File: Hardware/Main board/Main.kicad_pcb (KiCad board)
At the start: 2 copper layers, 65 x 56 mm, 24 parts, among them J1 RJ12, J10 Conn_01x03, J11 Conn_01x03, J13 Conn_01x04_Male, J14 Conn_01x04_Male, J2 AudioJack3, J3 AudioJack3, J4 AudioJack3, J5 AudioJack3, J6 RJ12, J7 RJ12, J8 Conn_01x03, J9 Conn_01x03, P1 Conn_02x20_Odd_Even, U1 ADS1115IDGS, U2 PCF8574

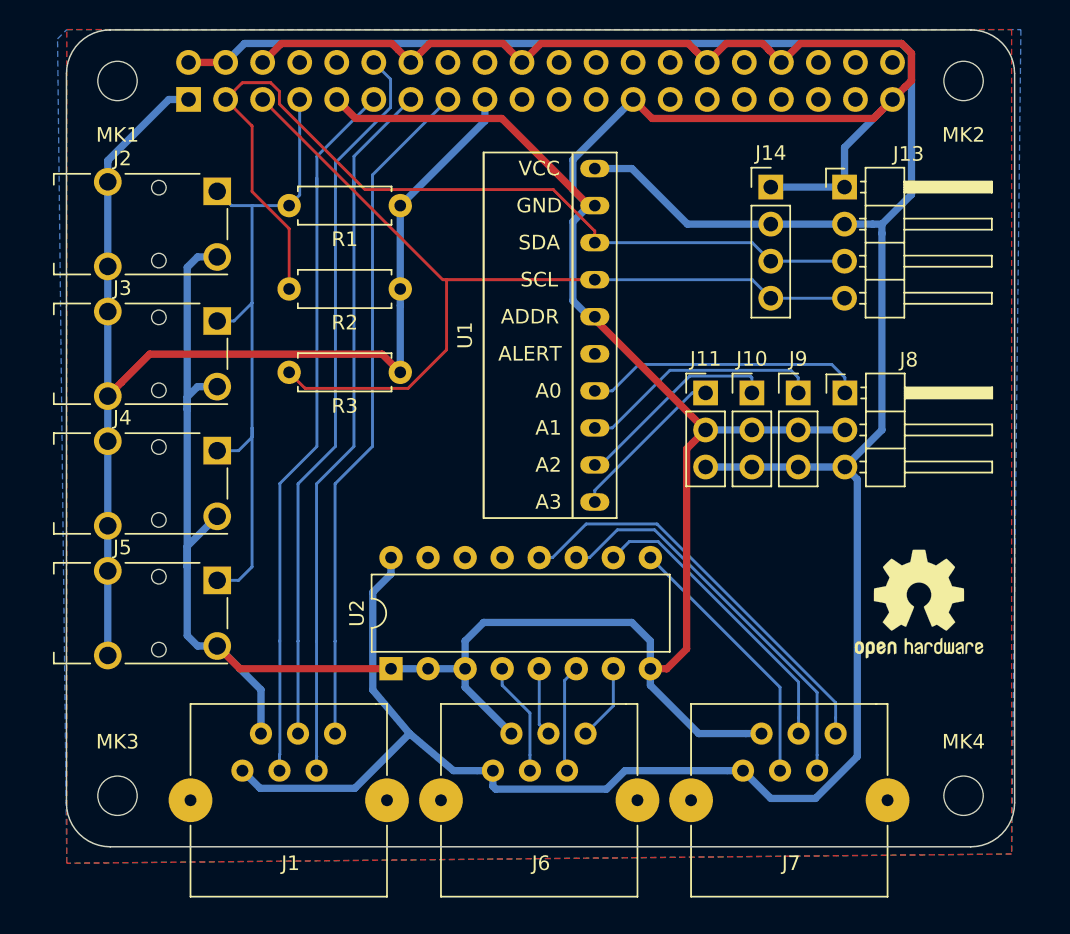
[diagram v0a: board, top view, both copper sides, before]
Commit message: Poprawki w płycie głównej
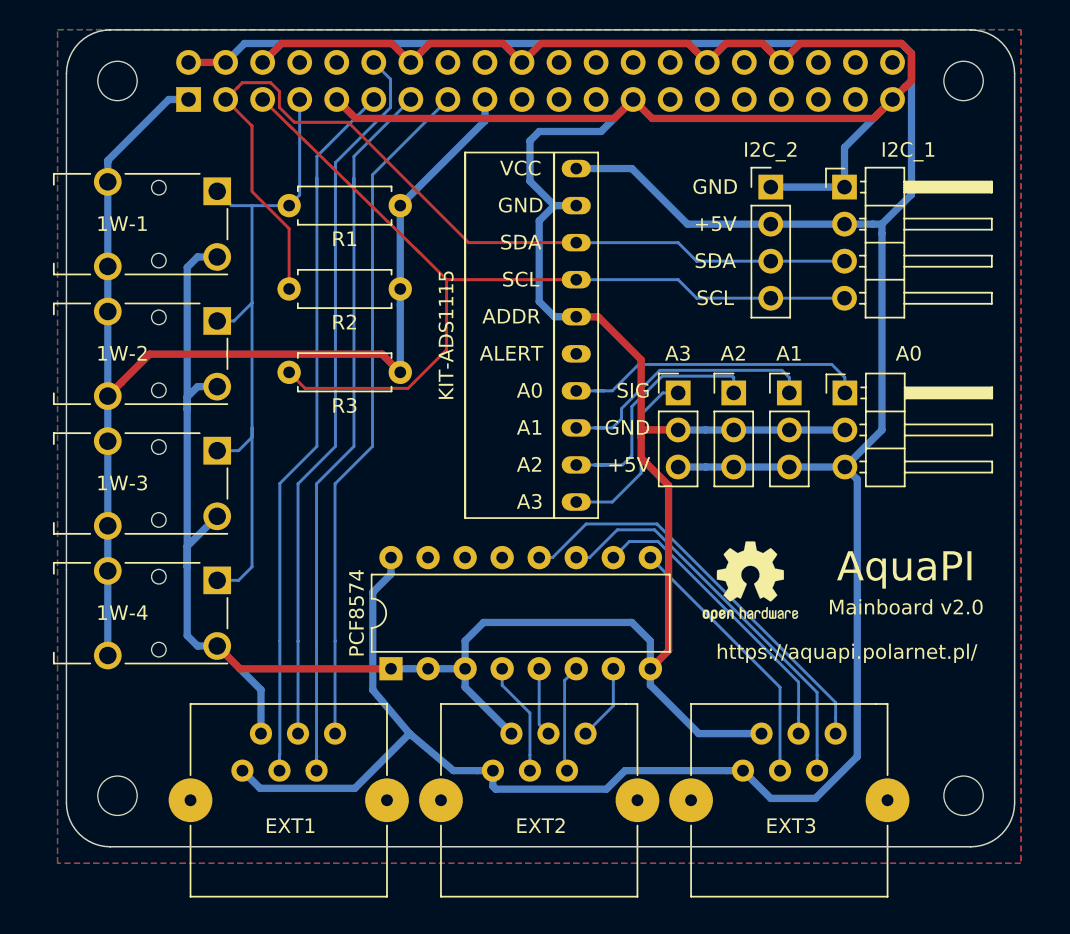
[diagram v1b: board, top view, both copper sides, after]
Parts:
- removed J6: RJ12, Connectors:RJ12_E
- removed the REF*** at (258.4, 133.3)
- added EXT2: RJ12, Connectors:RJ12_E, F.Cu at (229.2, 144.8)
- added REF***: OSHW-Logo2_7.3x6mm_SilkScreen, Symbols:OSHW-Logo2_7.3x6mm_SilkScreen, F.Cu at (246.9, 131.8)
- A0: renamed from J8; value Conn_01x03 -> ADC_A
- A1: renamed from J9; value Conn_01x03 -> ADC_B
- A2: renamed from J10; value Conn_01x03 -> ADC_C
- A3: renamed from J11; value Conn_01x03 -> ADC_D
- moved A3 1.88 mm to (241.9, 118.9)
- moved KIT-ADS1115 1.27 mm to (234.9, 114.9)
- moved A2 1.25 mm to (245.7, 118.9)
- moved A1 0.61 mm to (249.6, 118.9)
- renumbered J2 to 1W-1, J3 to 1W-2, J4 to 1W-3, J5 to 1W-4, J1 to EXT1, J7 to EXT3, J13 to I2C_1, J14 to I2C_2, U1 to KIT-ADS1115, U2 to PCF8574
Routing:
- net GND: track 258.9 -> 269.5 mm
- net Net-(A2-Pad1): track 14.4 -> 18.1 mm
- net +5V: track 193.9 -> 197.1 mm
- net Net-(A0-Pad1): track 19.3 -> 21.2 mm
- net Net-(A1-Pad1): track 16.8 -> 18.5 mm
- net Net-(A3-Pad1): track 11.2 -> 12.4 mm
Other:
- board text added: "+5V"
- board text added: "AquaPI"
- board text added: "GND"
- board text added: "Mainboard v2.0"
- board text added: "SCL"
- board text added: "SDA"
- board text added: "SIG"
- board text added: "https://aquapi.polarnet.pl/"

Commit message: nowy projekt sprzętu
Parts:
- removed 1W-1, 1W-2, 1W-3, 1W-4: AudioJack3, Connector_Audio:Jack_3.5mm_Switronic_ST-005-G_horizontal
- removed REF***: OSHW-Logo2_7.3x6mm_SilkScreen, Symbols:OSHW-Logo2_7.3x6mm_SilkScreen
- added J1: PJ-327, Main:PJ-327, F.Cu at (200.0, 116.0)
- added J2: PJ-327, Main:PJ-327, F.Cu at (200.0, 126.0)
- added J3: PJ-327, Main:PJ-327, F.Cu at (200.0, 106.0)
- added J4: Barrel_Jack_Switch, Main:DC-1GDC1.7_4.0K2, F.Cu at (198.5, 136.5)
- added R4: 4,7k, Resistors_THT:R_Axial_DIN0207_L6.3mm_D2.5mm_P7.62mm_Horizontal, F.Cu at (215.5, 128.5)
- EXT1, EXT2, EXT3: footprint Connectors:RJ12_E -> Main:RJ25_Wayconn_MJEA-660X1_Horizontal
- moved R3 22.8 mm to (242.0, 105.0), turned to 270 degrees
- moved R1 15.8 mm to (215.5, 120.0), turned to 90 degrees
- moved R2 15.7 mm to (237.0, 105.0), turned to 270 degrees
- moved EXT1 9.11 mm to (221.0, 143.0)
- moved EXT2 7.48 mm to (236.5, 143.0)
- moved EXT3 5.90 mm to (252.0, 143.0)
- moved KIT-ADS1115 3.45 mm to (231.5, 115.0)
- moved I2C_2 2.22 mm to (250.5, 104.8)
- moved A0 1.00 mm to (254.4, 118.9)
- moved A1 1.00 mm to (250.6, 118.9)
- moved A2 1.00 mm to (246.7, 118.9)
- moved A3 1.00 mm to (242.9, 118.9)
- moved I2C_1 1.00 mm to (254.3, 104.8)
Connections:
- I2C_1 pad 3: /GPIO2(SDA1) -> /GPIO3(SCL1)
- I2C_1 pad 4: /GPIO3(SCL1) -> /GPIO2(SDA1)
- I2C_2 pad 3: /GPIO2(SDA1) -> /GPIO3(SCL1)
- I2C_2 pad 4: /GPIO3(SCL1) -> /GPIO2(SDA1)
- P1 pad 16: (no net) -> /GPIO23(GEN4)
- PCF8574 pad 14: (no net) -> /GPIO3(SCL1)
- PCF8574 pad 15: (no net) -> /GPIO2(SDA1)
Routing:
- net /GPIO23(GEN4): track 0.00 -> 67.0 mm
- net GND: track 269.5 -> 317.2 mm, vias 0 -> 10
- net +3V3: track 84.1 -> 103.6 mm
- net +5V: track 197.1 -> 214.3 mm
- net /GPIO3(SCL1): track 62.6 -> 77.3 mm
- net /GPIO2(SDA1): track 63.4 -> 73.9 mm
- net Net-(EXT2-Pad4): track 4.71 -> 14.5 mm
- net Net-(EXT2-Pad6): track 5.23 -> 14.2 mm
- net Net-(EXT3-Pad6): track 28.5 -> 22.0 mm
- net Net-(EXT3-Pad5): track 27.3 -> 21.6 mm
- net /GPIO22(GEN3): track 46.7 -> 51.6 mm, vias 0 -> 2
- net /GPIO17(GEN0): track 49.3 -> 45.1 mm, vias 0 -> 1
- net Net-(A0-Pad1): track 21.2 -> 24.9 mm
- net Net-(A1-Pad1): track 18.5 -> 21.8 mm
- net /GPIO27(GEN2): track 50.4 -> 47.6 mm, vias 0 -> 2
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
